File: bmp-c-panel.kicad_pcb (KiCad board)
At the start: 2 copper layers, 77 x 86 mm, 512 parts, among them J1 TYPE-C-31-M-12, J3 FTSH-107-01-F-DV-K, Q1 DMG1023UV, Q2 DMG1024UV, SW1 B3U-1000P, U1 USBLC6-2P6, U2 74LVC2T45GT, U3 74LVC2T45GT, U4 74LVC2T45GT, U5 74LVC2T45GT, U6 STM32F103CBU, U7 TLV70033DCK, Y1 CSTNE8M00G520000R0

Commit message: Fix up known issues.
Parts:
- removed the LOGO1 at (77.2, 28.2)
- removed the LOGO1 at (77.2, 46.8)
- removed the LOGO1 at (77.2, 65.2)
- removed the LOGO1 at (77.2, 83.8)
- removed the LOGO1 at (25.8, 83.8)
- removed the LOGO1 at (25.8, 65.2)
- removed the LOGO1 at (25.8, 46.8)
- removed the LOGO1 at (25.8, 28.2)
- removed the REF** at (83.0, 96.5)
- removed the REF** at (83.0, 15.5)
- removed the REF** at (20.0, 15.5)
- removed the REF** at (15.5, 96.5)
- removed the REF** at (87.5, 15.5)
- removed the REF** at (15.5, 15.5)
- added LOGO1: Logo_Open_Hardware_Small, Symbol:OSHW-Symbol_6.7x6mm_SilkScreen, B.Cu at (26.1, 28.2)
- added LOGO1: Logo_Open_Hardware_Small, Symbol:OSHW-Symbol_6.7x6mm_SilkScreen, B.Cu at (26.1, 46.8)
- added LOGO1: Logo_Open_Hardware_Small, Symbol:OSHW-Symbol_6.7x6mm_SilkScreen, B.Cu at (26.1, 65.2)
- added LOGO1: Logo_Open_Hardware_Small, Symbol:OSHW-Symbol_6.7x6mm_SilkScreen, B.Cu at (26.1, 83.8)
- added LOGO1: Logo_Open_Hardware_Small, Symbol:OSHW-Symbol_6.7x6mm_SilkScreen, B.Cu at (77.0, 28.2)
- added LOGO1: Logo_Open_Hardware_Small, Symbol:OSHW-Symbol_6.7x6mm_SilkScreen, B.Cu at (77.0, 46.8)
- added LOGO1: Logo_Open_Hardware_Small, Symbol:OSHW-Symbol_6.7x6mm_SilkScreen, B.Cu at (77.0, 65.2)
- added LOGO1: Logo_Open_Hardware_Small, Symbol:OSHW-Symbol_6.7x6mm_SilkScreen, B.Cu at (77.0, 83.8)
- added REF**: Fiducial_0.5mm_Mask1.5mm, Fiducial:Fiducial_0.5mm_Mask1.5mm, F.Cu at (82.0, 96.5)
- added REF**: Fiducial_0.5mm_Mask1.5mm, Fiducial:Fiducial_0.5mm_Mask1.5mm, F.Cu at (82.0, 15.5)
- added REF**: Fiducial_0.5mm_Mask1.5mm, Fiducial:Fiducial_0.5mm_Mask1.5mm, F.Cu at (21.0, 15.5)
- added REF**: MountingHole_3mm, MountingHole:MountingHole_3mm, F.Cu at (16.5, 96.0)
- added REF**: MountingHole_3mm, MountingHole:MountingHole_3mm, F.Cu at (86.5, 16.0)
- added REF**: MountingHole_3mm, MountingHole:MountingHole_3mm, F.Cu at (16.5, 16.0)
- D2 (x8): value LED GREEN -> LED BLUE
- D3 (x8): value LED ORANGE -> LED GREEN
- FB1 (x8): value Ferrite_Bead_Small -> 330R @ 100MHz
- moved REF** 1.12 mm to (86.5, 96.0)
- moved REF** 1.00 mm to (21.0, 96.5)
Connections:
- C1 pad 1: (no net) -> +3V3 (x7)
- C1 pad 2: (no net) -> GND (x7)
- C11 pad 1: (no net) -> /iTPWR (x7)
- C11 pad 2: (no net) -> GND (x7)
- C12 pad 1: (no net) -> Net-(C12-Pad1) (x7)
- C12 pad 2: (no net) -> GND (x7)
- C13 pad 1: (no net) -> GND (x7)
- C13 pad 2: (no net) -> /xTPWR (x7)
- C15 pad 1: (no net) -> +3V3 (x7)
- C15 pad 2: (no net) -> GND (x7)
- C16 pad 1: (no net) -> GND (x7)
- C16 pad 2: (no net) -> +3V3 (x7)
- C17 pad 1: (no net) -> GND (x7)
- C17 pad 2: (no net) -> +3V3 (x7)
- C18 pad 1: (no net) -> GND (x7)
- C18 pad 2: (no net) -> +3V3 (x7)
- C19 pad 1: (no net) -> GND (x7)
- C19 pad 2: (no net) -> /xTPWR (x7)
- C20 pad 1: (no net) -> GND (x7)
- C20 pad 2: (no net) -> +3V3 (x7)
- C21 pad 1: (no net) -> GND (x7)
- C21 pad 2: (no net) -> +3V3 (x7)
- C3 pad 1: (no net) -> +3V3 (x7)
- C3 pad 2: (no net) -> GND (x7)
- C4 pad 1: (no net) -> GND (x7)
- C4 pad 2: (no net) -> /xTPWR (x7)
- C5 pad 1: (no net) -> +5V (x7)
- C5 pad 2: (no net) -> GND (x7)
- C6 pad 1: (no net) -> +3V3 (x7)
- C6 pad 2: (no net) -> GND (x7)
- C7 pad 1: (no net) -> +5V (x7)
- C7 pad 2: (no net) -> GND (x7)
- C8 pad 1: (no net) -> GND (x7)
- C8 pad 2: (no net) -> /xTPWR (x7)
- C9 pad 1: (no net) -> +3V3 (x7)
- C9 pad 2: (no net) -> GND (x7)
- D1 pad 1: (no net) -> GND (x7)
- D1 pad 2: (no net) -> Net-(D1-Pad2) (x7)
- D2 pad 1: (no net) -> GND (x7)
- D2 pad 2: (no net) -> Net-(D2-Pad2) (x7)
- D3 pad 1: (no net) -> GND (x7)
- D3 pad 2: (no net) -> Net-(D3-Pad2) (x7)
- D4 pad 1: (no net) -> GND (x7)
- D4 pad 2: (no net) -> Net-(D4-Pad2) (x7)
- FB1 pad 1: (no net) -> +5V (x7)
- FB1 pad 2: (no net) -> Net-(FB1-Pad2) (x7)
- J1 pad A1: (no net) -> GND (x7)
- J1 pad A12: (no net) -> GND (x7)
- J1 pad A4: (no net) -> Net-(FB1-Pad2) (x7)
- J1 pad A5: (no net) -> Net-(J1-PadA5) (x7)
- J1 pad A6: (no net) -> /USBX_p (x7)
- J1 pad A7: (no net) -> /USBX_n (x7)
- J1 pad A8: (no net) -> Net-(J1-PadA8) (x7)
- J1 pad A9: (no net) -> Net-(FB1-Pad2) (x7)
- J1 pad B1: (no net) -> GND (x7)
- J1 pad B12: (no net) -> GND (x7)
- J1 pad B4: (no net) -> Net-(FB1-Pad2) (x7)
- J1 pad B5: (no net) -> Net-(J1-PadB5) (x7)
- J1 pad B6: (no net) -> /USBX_p (x7)
- J1 pad B7: (no net) -> /USBX_n (x7)
- J1 pad B8: (no net) -> Net-(J1-PadB8) (x7)
- J1 pad B9: (no net) -> Net-(FB1-Pad2) (x7)
- J1 pad S1: (no net) -> Net-(J1-PadS1) (x7)
- J3 pad 1: (no net) -> Net-(J3-Pad1) (x7)
- J3 pad 10: (no net) -> /TDI (x7)
- J3 pad 11: (no net) -> GND (x7)
- J3 pad 12: (no net) -> /RST (x7)
- J3 pad 13: (no net) -> /TXD (x7)
- J3 pad 14: (no net) -> /RXD (x7)
- J3 pad 2: (no net) -> Net-(J3-Pad2) (x7)
- J3 pad 3: (no net) -> /TPWR (x7)
- J3 pad 4: (no net) -> /TMS (x7)
- J3 pad 5: (no net) -> GND (x7)
- J3 pad 6: (no net) -> /TCK (x7)
- J3 pad 7: (no net) -> GND (x7)
- J3 pad 8: (no net) -> /TDO (x7)
- J3 pad 9: (no net) -> Net-(J3-Pad9) (x7)
- Q1 pad 1: (no net) -> Net-(Q1-Pad1) (x7)
- Q1 pad 2: (no net) -> /PWR_BR (x7)
- Q1 pad 3: (no net) -> /TPWR (x7)
- Q1 pad 4: (no net) -> Net-(Q1-Pad1) (x7)
- Q1 pad 5: (no net) -> /PWR_BR (x7)
- Q1 pad 6: (no net) -> +3V3 (x7)
- Q2 pad 1: (no net) -> GND (x7)
- Q2 pad 2: (no net) -> /iRST (x7)
- Q2 pad 3: (no net) -> /iRST_SENSE (x7)
- Q2 pad 4: (no net) -> GND (x7)
- Q2 pad 5: (no net) -> /xRST (x7)
- Q2 pad 6: (no net) -> /xRST (x7)
- R1 pad 1: (no net) -> GND (x7)
- R1 pad 2: (no net) -> Net-(J1-PadA5) (x7)
- R10 pad 1: (no net) -> /USBi_p (x7)
- R10 pad 2: (no net) -> Net-(R10-Pad2) (x7)
- R11 pad 1: (no net) -> /xRST (x7)
- R11 pad 2: (no net) -> /xTPWR (x7)
- R12 pad 1: (no net) -> /PWR_BR (x7)
- R12 pad 2: (no net) -> Net-(Q1-Pad1) (x7)
- R2 pad 1: (no net) -> GND (x7)
- R2 pad 2: (no net) -> Net-(J1-PadB5) (x7)
- R3 pad 1: (no net) -> /VBUS (x7)
- R3 pad 2: (no net) -> GND (x7)
- R4 pad 1: (no net) -> +5V (x7)
- R4 pad 2: (no net) -> /VBUS (x7)
- R5 pad 1: (no net) -> /USBi_n (x7)
- R5 pad 2: (no net) -> Net-(R5-Pad2) (x7)
- R6 pad 1: (no net) -> /USBi_p (x7)
- R6 pad 2: (no net) -> Net-(R6-Pad2) (x7)
- R7 pad 1: (no net) -> /iTPWR (x7)
- R7 pad 2: (no net) -> GND (x7)
- R8 pad 1: (no net) -> Net-(R8-Pad1) (x7)
- R8 pad 2: (no net) -> +3V3 (x7)
- R9 pad 1: (no net) -> /xTPWR (x7)
- R9 pad 2: (no net) -> /iTPWR (x7)
- RN1 pad 1: (no net) -> +3V3 (x7)
- RN1 pad 2: (no net) -> /LED2 (x7)
- RN1 pad 3: (no net) -> /LED1 (x7)
- RN1 pad 4: (no net) -> /LED0 (x7)
- RN1 pad 5: (no net) -> Net-(D4-Pad2) (x7)
- RN1 pad 6: (no net) -> Net-(D3-Pad2) (x7)
- RN1 pad 7: (no net) -> Net-(D1-Pad2) (x7)
- RN1 pad 8: (no net) -> Net-(D2-Pad2) (x7)
- RN2 pad 1: (no net) -> /RST (x7)
- RN2 pad 2: (no net) -> /RXD (x7)
- RN2 pad 3: (no net) -> /TMS (x7)
- RN2 pad 4: (no net) -> /TPWR (x7)
- RN2 pad 5: (no net) -> /xTPWR (x7)
- RN2 pad 6: (no net) -> /xTMS (x7)
- RN2 pad 7: (no net) -> /xRXD (x7)
- RN2 pad 8: (no net) -> /xRST (x7)
- RN3 pad 1: (no net) -> /TDO (x7)
- RN3 pad 2: (no net) -> /TDI (x7)
- RN3 pad 3: (no net) -> /TCK (x7)
- RN3 pad 4: (no net) -> /TXD (x7)
- RN3 pad 5: (no net) -> /xTXD (x7)
- RN3 pad 6: (no net) -> /xTCK (x7)
- RN3 pad 7: (no net) -> /xTDI (x7)
- RN3 pad 8: (no net) -> /xTDO (x7)
- SW1 pad 1: (no net) -> GND (x7)
- SW1 pad 2: (no net) -> Net-(R8-Pad1) (x7)
- TP1 pad 1: (no net) -> +3V3 (x7)
- TP2 pad 1: (no net) -> GND (x7)
- TP4 pad 1: (no net) -> Net-(C12-Pad1) (x7)
- TP5 pad 1: (no net) -> /SWDIO (x7)
- TP6 pad 1: (no net) -> /SWCLK (x7)
- U1 pad 1: (no net) -> /USBX_n (x7)
- U1 pad 2: (no net) -> GND (x7)
- U1 pad 3: (no net) -> /USBX_p (x7)
- U1 pad 4: (no net) -> Net-(R6-Pad2) (x7)
- U1 pad 5: (no net) -> +5V (x7)
- U1 pad 6: (no net) -> Net-(R5-Pad2) (x7)
- U2 pad 1: (no net) -> +3V3 (x7)
- U2 pad 2: (no net) -> GND (x7)
- U2 pad 3: (no net) -> /iTXD (x7)
- U2 pad 4: (no net) -> GND (x7)
- U2 pad 5: (no net) -> +3V3 (x7)
- U2 pad 6: (no net) -> /xTXD (x7)
- U2 pad 7: (no net) -> GND (x7)
- U2 pad 8: (no net) -> /xTPWR (x7)
- U3 pad 1: (no net) -> +3V3 (x7)
- U3 pad 2: (no net) -> /iTCK (x7)
- U3 pad 3: (no net) -> /iTDI (x7)
- U3 pad 4: (no net) -> GND (x7)
- U3 pad 5: (no net) -> +3V3 (x7)
- U3 pad 6: (no net) -> /xTDI (x7)
- U3 pad 7: (no net) -> /xTCK (x7)
- U3 pad 8: (no net) -> /xTPWR (x7)
- U4 pad 1: (no net) -> +3V3 (x7)
- U4 pad 2: (no net) -> /iTDO (x7)
- U4 pad 3: (no net) -> /iRXD (x7)
- U4 pad 4: (no net) -> GND (x7)
- U4 pad 5: (no net) -> GND (x7)
- U4 pad 6: (no net) -> /xRXD (x7)
- U4 pad 7: (no net) -> /xTDO (x7)
- U4 pad 8: (no net) -> /xTPWR (x7)
- U5 pad 1: (no net) -> +3V3 (x7)
- U5 pad 2: (no net) -> GND (x7)
- U5 pad 3: (no net) -> /iTMS (x7)
- U5 pad 4: (no net) -> GND (x7)
- U5 pad 5: (no net) -> /iTMS_DIR (x7)
- U5 pad 6: (no net) -> /xTMS (x7)
- U5 pad 7: (no net) -> GND (x7)
- U5 pad 8: (no net) -> /xTPWR (x7)
- U6 pad 1: (no net) -> +3V3 (x7)
- U6 pad 10: (no net) -> Net-(U6-Pad10) (x7)
- U6 pad 11: (no net) -> /iTMS_DIR (x7)
- U6 pad 12: (no net) -> /iRST (x7)
- U6 pad 13: (no net) -> /iTDI (x7)
- U6 pad 14: (no net) -> /iTMS (x7)
- U6 pad 15: (no net) -> /iTCK (x7)
- U6 pad 16: (no net) -> /iTDO (x7)
- U6 pad 17: (no net) -> /iRST_SENSE (x7)
- U6 pad 18: (no net) -> /iTPWR (x7)
- U6 pad 19: (no net) -> /PWR_BR (x7)
- U6 pad 2: (no net) -> Net-(U6-Pad2) (x7)
- U6 pad 20: (no net) -> /LED0 (x7)
- U6 pad 21: (no net) -> /LED1 (x7)
- U6 pad 22: (no net) -> /LED2 (x7)
- U6 pad 23: (no net) -> GND (x7)
- U6 pad 24: (no net) -> +3V3 (x7)
- U6 pad 25: (no net) -> Net-(R8-Pad1) (x7)
- U6 pad 26: (no net) -> /VBUS (x7)
- U6 pad 27: (no net) -> Net-(U6-Pad27) (x7)
- U6 pad 28: (no net) -> Net-(U6-Pad28) (x7)
- U6 pad 29: (no net) -> Net-(R10-Pad2) (x7)
- U6 pad 3: (no net) -> Net-(U6-Pad3) (x7)
- U6 pad 30: (no net) -> /iTXD (x7)
- U6 pad 31: (no net) -> /iRXD (x7)
- U6 pad 32: (no net) -> /USBi_n (x7)
- U6 pad 33: (no net) -> /USBi_p (x7)
- U6 pad 34: (no net) -> /SWDIO (x7)
- U6 pad 35: (no net) -> GND (x7)
- U6 pad 36: (no net) -> +3V3 (x7)
- U6 pad 37: (no net) -> /SWCLK (x7)
- U6 pad 38: (no net) -> Net-(U6-Pad38) (x7)
- U6 pad 39: (no net) -> Net-(U6-Pad39) (x7)
- U6 pad 4: (no net) -> Net-(U6-Pad4) (x7)
- U6 pad 40: (no net) -> +3V3 (x7)
- U6 pad 41: (no net) -> +3V3 (x7)
- U6 pad 42: (no net) -> +3V3 (x7)
- U6 pad 43: (no net) -> Net-(U6-Pad43) (x7)
- U6 pad 44: (no net) -> GND (x7)
- U6 pad 45: (no net) -> Net-(U6-Pad45) (x7)
- U6 pad 46: (no net) -> Net-(U6-Pad46) (x7)
- U6 pad 47: (no net) -> GND (x7)
- U6 pad 48: (no net) -> +3V3 (x7)
- U6 pad 49: (no net) -> GND (x7)
- U6 pad 5: (no net) -> Net-(U6-Pad5) (x7)
- U6 pad 6: (no net) -> Net-(U6-Pad6) (x7)
- U6 pad 7: (no net) -> Net-(C12-Pad1) (x7)
- U6 pad 8: (no net) -> GND (x7)
- U6 pad 9: (no net) -> +3V3 (x7)
- U7 pad 1: (no net) -> +5V (x7)
- U7 pad 2: (no net) -> GND (x7)
- U7 pad 3: (no net) -> +5V (x7)
- U7 pad 4: (no net) -> Net-(U7-Pad4) (x7)
- U7 pad 5: (no net) -> +3V3 (x7)
- Y1 pad 1: (no net) -> Net-(U6-Pad6) (x7)
- Y1 pad 2: (no net) -> GND (x7)
- Y1 pad 3: (no net) -> Net-(U6-Pad5) (x7)
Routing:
- net (no net): track 4864.6 -> 0.00 mm, vias 665 -> 0
- net +3V3: track 134.0 -> 1072.0 mm, vias 10 -> 80
- net GND: track 89.1 -> 712.5 mm, vias 42 -> 336
- net /iTXD: track 44.8 -> 358.7 mm, vias 4 -> 32
- net /xTPWR: track 34.9 -> 279.0 mm, vias 7 -> 56
- net Net-(R8-Pad1): track 28.6 -> 228.8 mm, vias 2 -> 16
- net Net-(C12-Pad1): track 27.6 -> 220.7 mm, vias 2 -> 16
- net /iRXD: track 26.4 -> 211.3 mm, vias 4 -> 32
- net /PWR_BR: track 25.9 -> 207.3 mm, vias 2 -> 16
- net +5V: track 16.4 -> 131.4 mm, vias 2 -> 16
- net /iRST_SENSE: track 16.3 -> 130.5 mm, vias 2 -> 16
- net /SWCLK: track 15.1 -> 120.5 mm, vias 1 -> 8
- net /RXD: track 13.6 -> 108.5 mm, vias 2 -> 16
- net /iRST: track 13.1 -> 105.0 mm, vias 2 -> 16
- net /RST: track 12.2 -> 97.2 mm, vias 2 -> 16
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- removed copper zone on B.Cu, net (none)

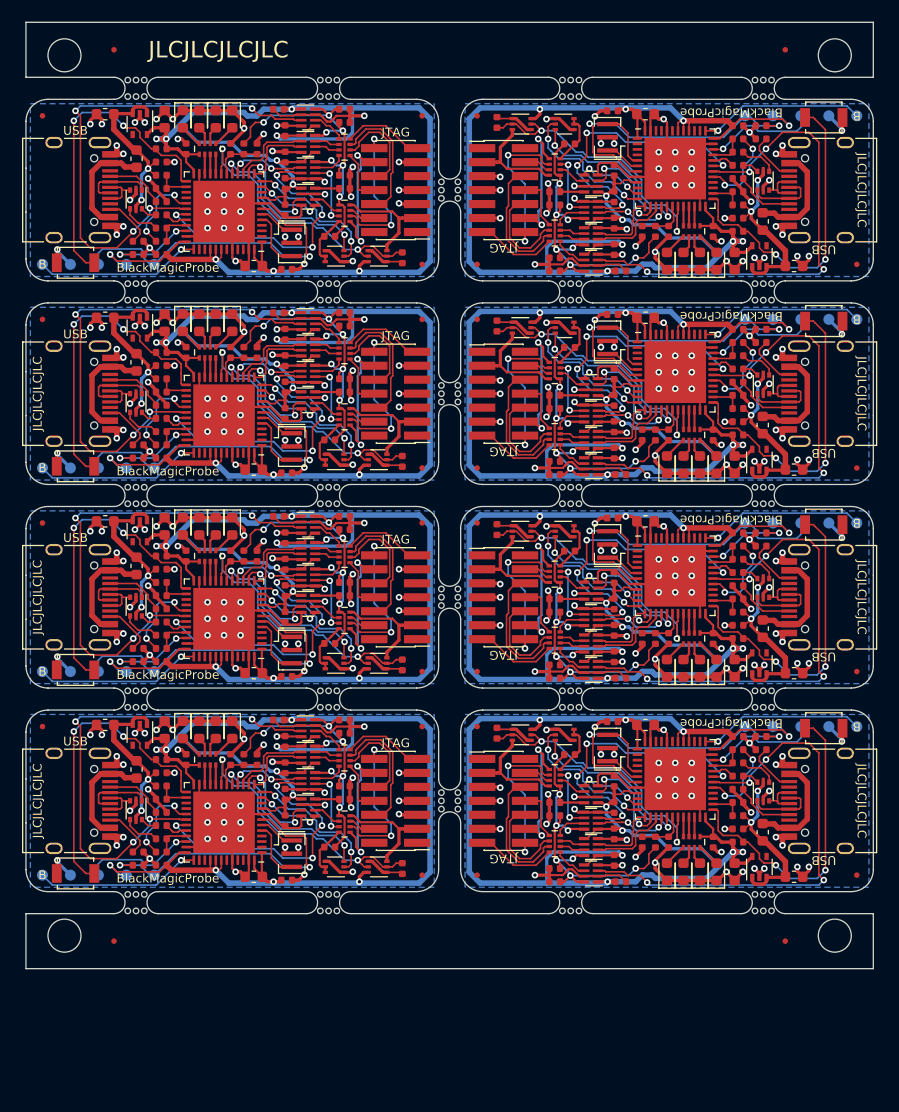
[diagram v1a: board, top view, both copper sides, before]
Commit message: Update alignment holes to be Stencil8 compatible.
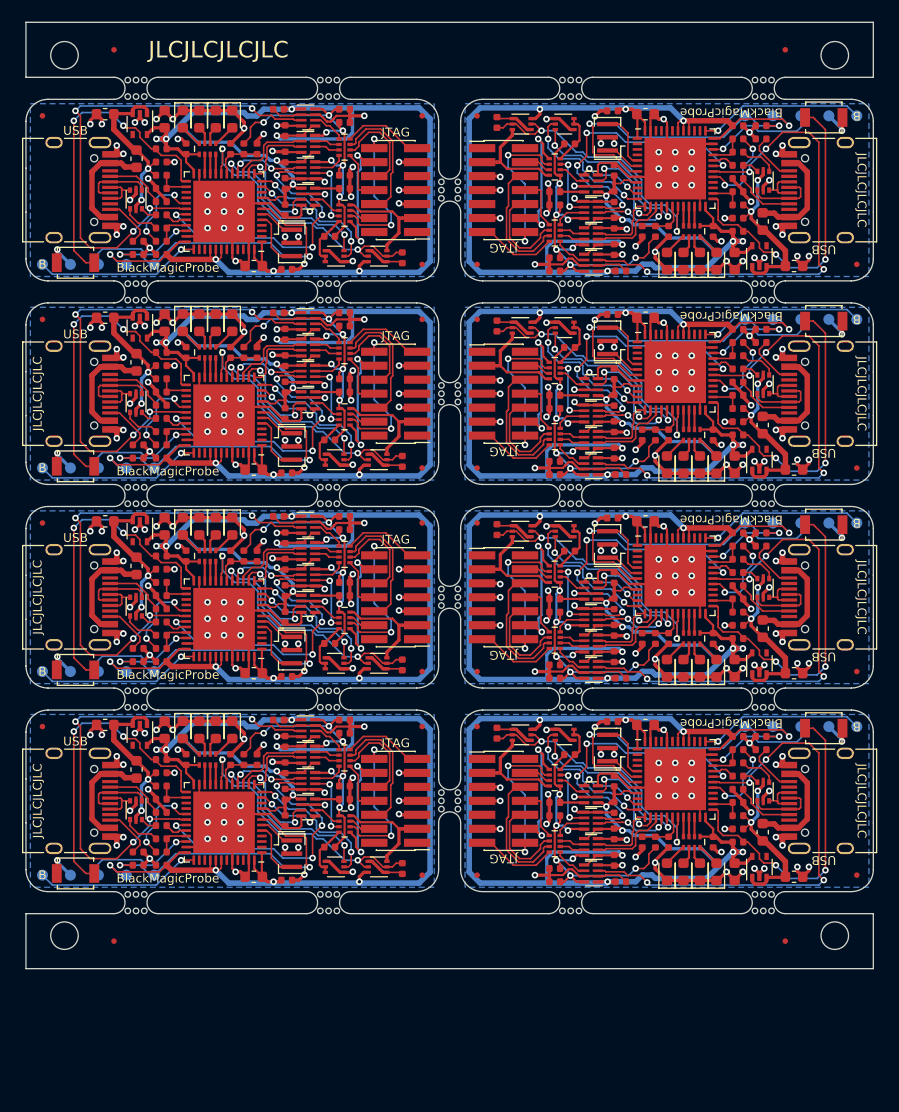
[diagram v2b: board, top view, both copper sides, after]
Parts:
- removed the REF** at (16.5, 96.0)
- removed the REF** at (86.5, 16.0)
- added REF**: MountingHole_2.5mm, MountingHole:MountingHole_2.5mm, F.Cu at (16.5, 96.0)
- added REF**: MountingHole_2.5mm, MountingHole:MountingHole_2.5mm, F.Cu at (86.5, 16.0)
- REF** (x2): value MountingHole_3mm -> MountingHole_2.5mm; footprint MountingHole:MountingHole_3mm -> MountingHole:MountingHole_2.5mm

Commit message: Moved panel alignment holes for easier assembly.
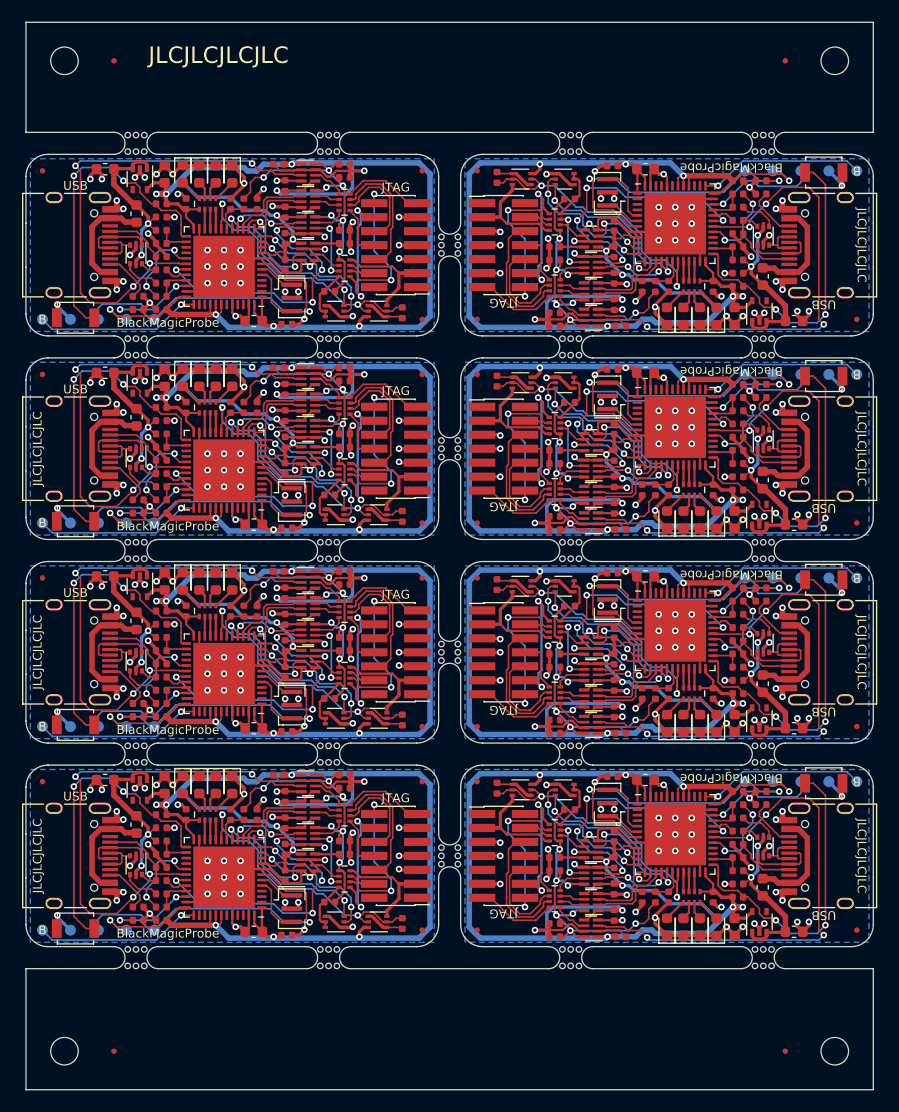
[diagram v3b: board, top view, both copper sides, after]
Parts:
- removed the C1 at (36.0, 39.4)
- removed the C1 at (36.0, 57.9)
- removed the C1 at (36.0, 76.4)
- removed the C1 at (67.0, 35.6)
- removed the C1 at (67.0, 54.1)
- removed the C1 at (67.0, 72.6)
- removed the C1 at (67.0, 91.1)
- removed the C11 at (31.6, 43.0)
- removed the C11 at (31.6, 61.5)
- removed the C11 at (31.6, 80.0)
- removed the C11 at (71.4, 32.0)
- removed the C11 at (71.4, 50.5)
- removed the C11 at (71.4, 69.0)
- removed the C11 at (71.4, 87.5)
- removed the C12 at (23.2, 52.6)
- removed the C12 at (23.2, 71.1)
- removed the C12 at (23.2, 89.6)
- removed the C12 at (79.8, 22.4)
- removed the C12 at (79.8, 40.9)
- removed the C12 at (79.8, 59.4)
- removed the C12 at (79.8, 77.9)
- removed the C13 at (42.0, 45.4)
- removed the C13 at (42.0, 63.9)
- removed the C13 at (42.0, 82.4)
- removed the C13 at (61.0, 29.6)
- removed the C13 at (61.0, 48.1)
- removed the C13 at (61.0, 66.6)
- removed the C13 at (61.0, 85.1)
- removed the C15 at (36.5, 46.1)
- removed the C15 at (36.5, 64.7)
- removed the C15 at (36.5, 83.2)
- removed the C15 at (66.5, 28.9)
- removed the C15 at (66.5, 47.4)
- removed the C15 at (66.5, 65.8)
- removed the C15 at (66.5, 84.3)
- removed the C16 at (25.3, 52.6)
- removed the C16 at (25.3, 71.1)
- removed the C16 at (25.3, 89.6)
- removed the C16 at (77.7, 22.4)
- removed the C16 at (77.7, 40.9)
- removed the C16 at (77.7, 59.4)
- removed the C16 at (77.7, 77.9)
- removed the C17 at (27.6, 43.0)
- removed the C17 at (27.6, 61.5)
- removed the C17 at (27.6, 80.0)
- removed the C17 at (75.5, 32.0)
- removed the C17 at (75.5, 50.5)
- removed the C17 at (75.5, 69.0)
- removed the C17 at (75.5, 87.5)
- removed the C18 at (36.5, 48.5)
- removed the C18 at (36.5, 67.0)
- removed the C18 at (36.5, 85.5)
- removed the C18 at (66.5, 26.4)
- removed the C18 at (66.5, 45.0)
- removed the C18 at (66.5, 63.5)
- removed the C18 at (66.5, 82.0)
- removed the C19 at (42.0, 46.6)
- removed the C19 at (42.0, 65.1)
- removed the C19 at (42.0, 83.6)
- removed the C19 at (61.0, 28.4)
- removed the C19 at (61.0, 46.9)
- removed the C19 at (61.0, 65.4)
- removed the C19 at (61.0, 83.9)
- removed the C20 at (36.7, 54.0)
- removed the C20 at (36.7, 72.5)
- removed the C20 at (36.7, 91.0)
- removed the C20 at (66.3, 21.1)
- removed the C20 at (66.3, 39.5)
- removed the C20 at (66.3, 58.0)
- removed the C20 at (66.3, 76.5)
- removed the C21 at (33.7, 53.6)
- removed the C21 at (33.7, 72.2)
- removed the C21 at (33.7, 90.7)
- removed the C21 at (69.3, 21.4)
- removed the C21 at (69.3, 39.9)
- removed the C21 at (69.3, 58.4)
- removed the C21 at (69.3, 76.8)
- removed the C3 at (25.6, 40.3)
- removed the C3 at (25.6, 58.8)
- removed the C3 at (25.6, 77.3)
- removed the C3 at (77.4, 34.7)
- removed the C3 at (77.4, 53.2)
- removed the C3 at (77.4, 71.7)
- removed the C3 at (77.4, 90.2)
- removed the C4 at (42.0, 39.4)
- removed the C4 at (42.0, 57.9)
- removed the C4 at (42.0, 76.4)
- removed the C4 at (61.0, 35.6)
- removed the C4 at (61.0, 54.1)
- removed the C4 at (61.0, 72.6)
- removed the C4 at (61.0, 91.1)
- removed the C5 at (25.3, 44.2)
- removed the C5 at (25.3, 62.7)
- removed the C5 at (25.3, 81.2)
- removed the C5 at (77.7, 30.8)
- removed the C5 at (77.7, 49.3)
- removed the C5 at (77.7, 67.8)
- removed the C5 at (77.7, 86.3)
- removed the C6 at (36.5, 41.4)
- removed the C6 at (36.5, 59.9)
- removed the C6 at (36.5, 78.3)
- removed the C6 at (66.5, 33.6)
- removed the C6 at (66.5, 52.1)
- removed the C6 at (66.5, 70.7)
- removed the C6 at (66.5, 89.2)
- removed the C7 at (20.2, 39.9)
- removed the C7 at (20.2, 58.4)
- removed the C7 at (20.2, 76.8)
- removed the C7 at (82.8, 35.1)
- removed the C7 at (82.8, 53.6)
- removed the C7 at (82.8, 72.2)
- removed the C7 at (82.8, 90.7)
- removed the C8 at (42.0, 40.6)
- removed the C8 at (42.0, 59.1)
- removed the C8 at (42.0, 77.6)
- removed the C8 at (61.0, 34.4)
- removed the C8 at (61.0, 52.9)
- removed the C8 at (61.0, 71.4)
- removed the C8 at (61.0, 89.9)
- removed the C9 at (36.5, 43.8)
- removed the C9 at (36.5, 62.2)
- removed the C9 at (36.5, 80.8)
- removed the C9 at (66.5, 31.2)
- removed the C9 at (66.5, 49.8)
- removed the C9 at (66.5, 68.2)
- removed the C9 at (66.5, 86.8)
- removed the D1 at (28.8, 40.3)
- removed the D1 at (28.8, 58.8)
- removed the D1 at (28.8, 77.3)
- removed the D1 at (74.2, 34.7)
- removed the D1 at (74.2, 53.2)
- removed the D1 at (74.2, 71.7)
- removed the D1 at (74.2, 90.2)
- removed the D2 at (27.2, 40.3)
- removed the D2 at (27.2, 58.8)
- removed the D2 at (27.2, 77.3)
- removed the D2 at (75.8, 34.7)
- removed the D2 at (75.8, 53.2)
- removed the D2 at (75.8, 71.7)
- removed the D2 at (75.8, 90.2)
- removed the D3 at (30.2, 40.3)
- removed the D3 at (30.2, 58.8)
- removed the D3 at (30.2, 77.3)
- removed the D3 at (72.8, 34.7)
- removed the D3 at (72.8, 53.2)
- removed the D3 at (72.8, 71.7)
- removed the D3 at (72.8, 90.2)
- removed the D4 at (31.8, 40.3)
- removed the D4 at (31.8, 58.8)
- removed the D4 at (31.8, 77.3)
- removed the D4 at (71.2, 34.7)
- removed the D4 at (71.2, 53.2)
- removed the D4 at (71.2, 71.7)
- removed the D4 at (71.2, 90.2)
- removed the FB1 at (23.1, 43.9)
- removed the FB1 at (23.1, 62.4)
- removed the FB1 at (23.1, 80.9)
- removed the FB1 at (80.0, 31.1)
- removed the FB1 at (80.0, 49.6)
- removed the FB1 at (80.0, 68.1)
- removed the FB1 at (80.0, 86.6)
- removed the FID1 at (14.5, 40.0)
- removed the FID1 at (14.5, 58.5)
- removed the FID1 at (14.5, 77.0)
- removed the FID1 at (88.5, 35.0)
- removed the FID1 at (88.5, 53.5)
- removed the FID1 at (88.5, 72.0)
- removed the FID1 at (88.5, 90.5)
- removed the FID2 at (49.0, 40.0)
- removed the FID2 at (49.0, 58.5)
- removed the FID2 at (49.0, 77.0)
- removed the FID2 at (54.0, 35.0)
- removed the FID2 at (54.0, 53.5)
- removed the FID2 at (54.0, 72.0)
- removed the FID2 at (54.0, 90.5)
- removed the FID3 at (49.0, 53.5)
- removed the FID3 at (49.0, 72.0)
- removed the FID3 at (49.0, 90.5)
- removed the FID3 at (54.0, 21.5)
- removed the FID3 at (54.0, 40.0)
- removed the FID3 at (54.0, 58.5)
- removed the FID3 at (54.0, 77.0)
- removed the J1 at (16.6, 46.8)
- removed the J1 at (16.6, 65.2)
- removed the J1 at (16.6, 83.8)
- removed the J1 at (86.4, 28.2)
- removed the J1 at (86.4, 46.8)
- removed the J1 at (86.4, 65.2)
- removed the J1 at (86.4, 83.8)
- removed the J3 at (46.6, 46.8)
- removed the J3 at (46.6, 65.2)
- removed the J3 at (46.6, 83.8)
- removed the J3 at (56.4, 28.2)
- removed the J3 at (56.4, 46.8)
- removed the J3 at (56.4, 65.2)
- removed the J3 at (56.4, 83.8)
- removed the LOGO1 at (26.1, 46.8)
- removed the LOGO1 at (26.1, 65.2)
- removed the LOGO1 at (26.1, 83.8)
- removed the LOGO1 at (77.0, 28.2)
- removed the LOGO1 at (77.0, 46.8)
- removed the LOGO1 at (77.0, 65.2)
- removed the LOGO1 at (77.0, 83.8)
- removed the Q1 at (45.0, 52.8)
- removed the Q1 at (45.0, 71.2)
- removed the Q1 at (45.0, 89.8)
- removed the Q1 at (58.0, 22.2)
- removed the Q1 at (58.0, 40.8)
- removed the Q1 at (58.0, 59.2)
- removed the Q1 at (58.0, 77.8)
- removed the Q2 at (41.0, 52.8)
- removed the Q2 at (41.0, 71.2)
- removed the Q2 at (41.0, 89.8)
- removed the Q2 at (62.0, 22.2)
- removed the Q2 at (62.0, 40.8)
- removed the Q2 at (62.0, 59.2)
- removed the Q2 at (62.0, 77.8)
- removed the R1 at (25.3, 47.8)
- removed the R1 at (25.3, 66.3)
- removed the R1 at (25.3, 84.8)
- removed the R1 at (77.7, 27.2)
- removed the R1 at (77.7, 45.7)
- removed the R1 at (77.7, 64.2)
- removed the R1 at (77.7, 82.7)
- removed the R10 at (25.3, 51.4)
- removed the R10 at (25.3, 69.9)
- removed the R10 at (25.3, 88.4)
- removed the R10 at (77.7, 23.6)
- removed the R10 at (77.7, 42.1)
- removed the R10 at (77.7, 60.6)
- removed the R10 at (77.7, 79.1)
- removed the R11 at (40.6, 51.0)
- removed the R11 at (40.6, 69.5)
- removed the R11 at (40.6, 88.0)
- removed the R11 at (62.4, 24.1)
- removed the R11 at (62.4, 42.5)
- removed the R11 at (62.4, 61.0)
- removed the R11 at (62.4, 79.5)
- removed the R12 at (47.2, 52.9)
- removed the R12 at (47.2, 71.4)
- removed the R12 at (47.2, 89.9)
- removed the R12 at (55.8, 22.1)
- removed the R12 at (55.8, 40.6)
- removed the R12 at (55.8, 59.1)
- removed the R12 at (55.8, 77.6)
- removed the R2 at (23.2, 51.4)
- removed the R2 at (23.2, 69.9)
- removed the R2 at (23.2, 88.4)
- removed the R2 at (79.8, 23.6)
- removed the R2 at (79.8, 42.1)
- removed the R2 at (79.8, 60.6)
- removed the R2 at (79.8, 79.1)
- removed the R3 at (25.3, 46.6)
- removed the R3 at (25.3, 65.1)
- removed the R3 at (25.3, 83.6)
- removed the R3 at (77.7, 28.4)
- removed the R3 at (77.7, 46.9)
- removed the R3 at (77.7, 65.4)
- removed the R3 at (77.7, 83.9)
- removed the R4 at (25.3, 45.4)
- removed the R4 at (25.3, 63.9)
- removed the R4 at (25.3, 82.4)
- removed the R4 at (77.7, 29.6)
- removed the R4 at (77.7, 48.1)
- removed the R4 at (77.7, 66.6)
- removed the R4 at (77.7, 85.1)
- removed the R5 at (25.3, 49.0)
- removed the R5 at (25.3, 67.5)
- removed the R5 at (25.3, 86.0)
- removed the R5 at (77.7, 26.0)
- removed the R5 at (77.7, 44.5)
- removed the R5 at (77.7, 63.0)
- removed the R5 at (77.7, 81.5)
- removed the R6 at (25.3, 50.2)
- removed the R6 at (25.3, 68.7)
- removed the R6 at (25.3, 87.2)
- removed the R6 at (77.7, 24.8)
- removed the R6 at (77.7, 43.3)
- removed the R6 at (77.7, 61.8)
- removed the R6 at (77.7, 80.3)
- removed the R7 at (34.0, 43.0)
- removed the R7 at (34.0, 61.5)
- removed the R7 at (34.0, 80.0)
- removed the R7 at (69.0, 32.0)
- removed the R7 at (69.0, 50.5)
- removed the R7 at (69.0, 69.0)
- removed the R7 at (69.0, 87.5)
- removed the R8 at (25.3, 43.0)
- removed the R8 at (25.3, 61.5)
- removed the R8 at (25.3, 80.0)
- removed the R8 at (77.7, 32.0)
- removed the R8 at (77.7, 50.5)
- removed the R8 at (77.7, 69.0)
- removed the R8 at (77.7, 87.5)
- removed the R9 at (32.8, 43.0)
- removed the R9 at (32.8, 61.5)
- removed the R9 at (32.8, 80.0)
- removed the R9 at (70.2, 32.0)
- removed the R9 at (70.2, 50.5)
- removed the R9 at (70.2, 69.0)
- removed the R9 at (70.2, 87.5)
- removed the REF** at (16.5, 96.0)
- removed the REF** at (86.5, 16.0)
- removed the REF** at (82.0, 96.5)
- removed the REF** at (82.0, 15.5)
- removed the REF** at (21.0, 15.5)
- removed the RN1 at (29.5, 43.0)
- removed the RN1 at (29.5, 61.5)
- removed the RN1 at (29.5, 80.0)
- removed the RN1 at (73.5, 32.0)
- removed the RN1 at (73.5, 50.5)
- removed the RN1 at (73.5, 69.0)
- removed the RN1 at (73.5, 87.5)
- removed the RN2 at (42.0, 48.9)
- removed the RN2 at (42.0, 67.3)
- removed the RN2 at (42.0, 85.8)
- removed the RN2 at (61.0, 26.1)
- removed the RN2 at (61.0, 44.6)
- removed the RN2 at (61.0, 63.1)
- removed the RN2 at (61.0, 81.7)
- removed the RN3 at (42.0, 42.9)
- removed the RN3 at (42.0, 61.4)
- removed the RN3 at (42.0, 79.8)
- removed the RN3 at (61.0, 32.1)
- removed the RN3 at (61.0, 50.6)
- removed the RN3 at (61.0, 69.2)
- removed the RN3 at (61.0, 87.7)
- removed the SW1 at (17.5, 53.4)
- removed the SW1 at (17.5, 71.8)
- removed the SW1 at (17.5, 90.3)
- removed the SW1 at (85.5, 21.6)
- removed the SW1 at (85.5, 40.1)
- removed the SW1 at (85.5, 58.6)
- removed the SW1 at (85.5, 77.2)
- removed the TP1 at (22.1, 53.5)
- removed the TP1 at (22.1, 72.0)
- removed the TP1 at (22.1, 90.5)
- removed the TP1 at (80.9, 21.5)
- removed the TP1 at (80.9, 40.0)
- removed the TP1 at (80.9, 58.5)
- removed the TP1 at (80.9, 77.0)
- removed the TP2 at (17.0, 53.5)
- removed the TP2 at (17.0, 72.0)
- removed the TP2 at (17.0, 90.5)
- removed the TP2 at (86.0, 21.5)
- removed the TP2 at (86.0, 40.0)
- removed the TP2 at (86.0, 58.5)
- removed the TP2 at (86.0, 77.0)
- removed the TP4 at (24.7, 53.5)
- removed the TP4 at (24.7, 72.0)
- removed the TP4 at (24.7, 90.5)
- removed the TP4 at (78.3, 21.5)
- removed the TP4 at (78.3, 40.0)
- removed the TP4 at (78.3, 58.5)
- removed the TP4 at (78.3, 77.0)
- removed the TP5 at (19.6, 53.5)
- removed the TP5 at (19.6, 72.0)
- removed the TP5 at (19.6, 90.5)
- removed the TP5 at (83.4, 21.5)
- removed the TP5 at (83.4, 40.0)
- removed the TP5 at (83.4, 58.5)
- removed the TP5 at (83.4, 77.0)
- removed the TP6 at (14.5, 53.5)
- removed the TP6 at (14.5, 72.0)
- removed the TP6 at (14.5, 90.5)
- removed the TP6 at (88.5, 21.5)
- removed the TP6 at (88.5, 40.0)
- removed the TP6 at (88.5, 58.5)
- removed the TP6 at (88.5, 77.0)
- removed the U1 at (23.0, 47.6)
- removed the U1 at (23.0, 66.1)
- removed the U1 at (23.0, 84.6)
- removed the U1 at (80.0, 27.4)
- removed the U1 at (80.0, 45.9)
- removed the U1 at (80.0, 64.4)
- removed the U1 at (80.0, 82.9)
- removed the U2 at (38.6, 40.1)
- removed the U2 at (38.6, 58.6)
- removed the U2 at (38.6, 77.2)
- removed the U2 at (64.3, 34.9)
- removed the U2 at (64.3, 53.4)
- removed the U2 at (64.3, 71.8)
- removed the U2 at (64.3, 90.3)
- removed the U3 at (38.6, 42.5)
- removed the U3 at (38.6, 61.0)
- removed the U3 at (38.6, 79.5)
- removed the U3 at (64.3, 32.5)
- removed the U3 at (64.3, 51.0)
- removed the U3 at (64.3, 69.5)
- removed the U3 at (64.3, 88.0)
- removed the U4 at (38.6, 45.0)
- removed the U4 at (38.6, 63.5)
- removed the U4 at (38.6, 82.0)
- removed the U4 at (64.3, 30.1)
- removed the U4 at (64.3, 48.5)
- removed the U4 at (64.3, 67.0)
- removed the U4 at (64.3, 85.5)
- removed the U5 at (38.6, 47.4)
- removed the U5 at (38.6, 65.8)
- removed the U5 at (38.6, 84.3)
- removed the U5 at (64.3, 27.6)
- removed the U5 at (64.3, 46.1)
- removed the U5 at (64.3, 64.7)
- removed the U5 at (64.3, 83.2)
- removed the U6 at (31.0, 48.7)
- removed the U6 at (31.0, 67.2)
- removed the U6 at (31.0, 85.7)
- removed the U6 at (72.0, 26.3)
- removed the U6 at (72.0, 44.8)
- removed the U6 at (72.0, 63.3)
- removed the U6 at (72.0, 81.8)
- removed the U7 at (23.4, 40.8)
- removed the U7 at (23.4, 59.2)
- removed the U7 at (23.4, 77.8)
- removed the U7 at (79.7, 34.2)
- removed the U7 at (79.7, 52.8)
- removed the U7 at (79.7, 71.2)
- removed the U7 at (79.7, 89.8)
- removed the Y1 at (37.1, 51.5)
- removed the Y1 at (37.1, 70.0)
- removed the Y1 at (37.1, 88.5)
- removed the Y1 at (65.8, 23.4)
- removed the Y1 at (65.8, 42.0)
- removed the Y1 at (65.8, 60.5)
- removed the Y1 at (65.8, 79.0)
- removed the mouse-bite-2mm-slot at (40.5, 74.5)
- removed the mouse-bite-2mm-slot at (23.0, 56.0)
- removed the mouse-bite-2mm-slot at (40.5, 56.0)
- removed the mouse-bite-2mm-slot at (51.5, 46.8)
- removed the mouse-bite-2mm-slot at (23.0, 37.5)
- removed the mouse-bite-2mm-slot at (40.5, 37.5)
- removed the mouse-bite-2mm-slot at (23.0, 93.0)
- removed the mouse-bite-2mm-slot at (62.5, 19.0)
- removed the mouse-bite-2mm-slot at (80.0, 19.0)
- removed the mouse-bite-2mm-slot at (40.5, 93.0)
- removed the mouse-bite-2mm-slot at (51.5, 83.8)
- removed the mouse-bite-2mm-slot at (23.0, 74.5)
- added C1: 100n, Capacitor_SMD:C_0402_1005Metric, F.Cu at (36.0, 44.4)
- added C1: 100n, Capacitor_SMD:C_0402_1005Metric, F.Cu at (36.0, 62.9)
- added C1: 100n, Capacitor_SMD:C_0402_1005Metric, F.Cu at (36.0, 81.4)
- added C1: 100n, Capacitor_SMD:C_0402_1005Metric, F.Cu at (67.0, 40.6)
- added C1: 100n, Capacitor_SMD:C_0402_1005Metric, F.Cu at (67.0, 59.1)
- added C1: 100n, Capacitor_SMD:C_0402_1005Metric, F.Cu at (67.0, 77.6)
- added C1: 100n, Capacitor_SMD:C_0402_1005Metric, F.Cu at (67.0, 96.1)
- added C11: 100n, Capacitor_SMD:C_0402_1005Metric, F.Cu at (31.6, 48.0)
- added C11: 100n, Capacitor_SMD:C_0402_1005Metric, F.Cu at (31.6, 66.5)
- added C11: 100n, Capacitor_SMD:C_0402_1005Metric, F.Cu at (31.6, 85.0)
- added C11: 100n, Capacitor_SMD:C_0402_1005Metric, F.Cu at (71.4, 37.0)
- added C11: 100n, Capacitor_SMD:C_0402_1005Metric, F.Cu at (71.4, 55.5)
- added C11: 100n, Capacitor_SMD:C_0402_1005Metric, F.Cu at (71.4, 74.0)
- added C11: 100n, Capacitor_SMD:C_0402_1005Metric, F.Cu at (71.4, 92.5)
- added C12: 100n, Capacitor_SMD:C_0402_1005Metric, F.Cu at (23.2, 57.6)
- added C12: 100n, Capacitor_SMD:C_0402_1005Metric, F.Cu at (23.2, 76.1)
- added C12: 100n, Capacitor_SMD:C_0402_1005Metric, F.Cu at (23.2, 94.6)
- added C12: 100n, Capacitor_SMD:C_0402_1005Metric, F.Cu at (79.8, 27.4)
- added C12: 100n, Capacitor_SMD:C_0402_1005Metric, F.Cu at (79.8, 45.9)
- added C12: 100n, Capacitor_SMD:C_0402_1005Metric, F.Cu at (79.8, 64.4)
- added C12: 100n, Capacitor_SMD:C_0402_1005Metric, F.Cu at (79.8, 82.9)
- added C13: 100n, Capacitor_SMD:C_0402_1005Metric, F.Cu at (42.0, 50.4)
- added C13: 100n, Capacitor_SMD:C_0402_1005Metric, F.Cu at (42.0, 68.9)
- added C13: 100n, Capacitor_SMD:C_0402_1005Metric, F.Cu at (42.0, 87.4)
- added C13: 100n, Capacitor_SMD:C_0402_1005Metric, F.Cu at (61.0, 34.6)
- added C13: 100n, Capacitor_SMD:C_0402_1005Metric, F.Cu at (61.0, 53.1)
- added C13: 100n, Capacitor_SMD:C_0402_1005Metric, F.Cu at (61.0, 71.6)
- added C13: 100n, Capacitor_SMD:C_0402_1005Metric, F.Cu at (61.0, 90.1)
- added C15: 100n, Capacitor_SMD:C_0402_1005Metric, F.Cu at (36.5, 51.1)
- added C15: 100n, Capacitor_SMD:C_0402_1005Metric, F.Cu at (36.5, 69.7)
- added C15: 100n, Capacitor_SMD:C_0402_1005Metric, F.Cu at (36.5, 88.2)
- added C15: 100n, Capacitor_SMD:C_0402_1005Metric, F.Cu at (66.5, 33.9)
- added C15: 100n, Capacitor_SMD:C_0402_1005Metric, F.Cu at (66.5, 52.4)
- added C15: 100n, Capacitor_SMD:C_0402_1005Metric, F.Cu at (66.5, 70.8)
- added C15: 100n, Capacitor_SMD:C_0402_1005Metric, F.Cu at (66.5, 89.3)
- added C16: 100n, Capacitor_SMD:C_0402_1005Metric, F.Cu at (25.3, 57.6)
- added C16: 100n, Capacitor_SMD:C_0402_1005Metric, F.Cu at (25.3, 76.1)
- added C16: 100n, Capacitor_SMD:C_0402_1005Metric, F.Cu at (25.3, 94.6)
- added C16: 100n, Capacitor_SMD:C_0402_1005Metric, F.Cu at (77.7, 27.4)
- added C16: 100n, Capacitor_SMD:C_0402_1005Metric, F.Cu at (77.7, 45.9)
- added C16: 100n, Capacitor_SMD:C_0402_1005Metric, F.Cu at (77.7, 64.4)
- added C16: 100n, Capacitor_SMD:C_0402_1005Metric, F.Cu at (77.7, 82.9)
- added C17: 100n, Capacitor_SMD:C_0402_1005Metric, F.Cu at (27.6, 48.0)
- added C17: 100n, Capacitor_SMD:C_0402_1005Metric, F.Cu at (27.6, 66.5)
- added C17: 100n, Capacitor_SMD:C_0402_1005Metric, F.Cu at (27.6, 85.0)
- added C17: 100n, Capacitor_SMD:C_0402_1005Metric, F.Cu at (75.5, 37.0)
- added C17: 100n, Capacitor_SMD:C_0402_1005Metric, F.Cu at (75.5, 55.5)
- added C17: 100n, Capacitor_SMD:C_0402_1005Metric, F.Cu at (75.5, 74.0)
- added C17: 100n, Capacitor_SMD:C_0402_1005Metric, F.Cu at (75.5, 92.5)
- added C18: 100n, Capacitor_SMD:C_0402_1005Metric, F.Cu at (36.5, 53.5)
- added C18: 100n, Capacitor_SMD:C_0402_1005Metric, F.Cu at (36.5, 72.0)
- added C18: 100n, Capacitor_SMD:C_0402_1005Metric, F.Cu at (36.5, 90.5)
- added C18: 100n, Capacitor_SMD:C_0402_1005Metric, F.Cu at (66.5, 31.4)
- added C18: 100n, Capacitor_SMD:C_0402_1005Metric, F.Cu at (66.5, 50.0)
- added C18: 100n, Capacitor_SMD:C_0402_1005Metric, F.Cu at (66.5, 68.5)
- added C18: 100n, Capacitor_SMD:C_0402_1005Metric, F.Cu at (66.5, 87.0)
- added C19: 100n, Capacitor_SMD:C_0402_1005Metric, F.Cu at (42.0, 51.6)
- added C19: 100n, Capacitor_SMD:C_0402_1005Metric, F.Cu at (42.0, 70.1)
- added C19: 100n, Capacitor_SMD:C_0402_1005Metric, F.Cu at (42.0, 88.6)
- added C19: 100n, Capacitor_SMD:C_0402_1005Metric, F.Cu at (61.0, 33.4)
- added C19: 100n, Capacitor_SMD:C_0402_1005Metric, F.Cu at (61.0, 51.9)
- added C19: 100n, Capacitor_SMD:C_0402_1005Metric, F.Cu at (61.0, 70.4)
- added C19: 100n, Capacitor_SMD:C_0402_1005Metric, F.Cu at (61.0, 88.9)
- added C20: 100n, Capacitor_SMD:C_0402_1005Metric, F.Cu at (36.7, 59.0)
- added C20: 100n, Capacitor_SMD:C_0402_1005Metric, F.Cu at (36.7, 77.5)
- added C20: 100n, Capacitor_SMD:C_0402_1005Metric, F.Cu at (36.7, 96.0)
- added C20: 100n, Capacitor_SMD:C_0402_1005Metric, F.Cu at (66.3, 26.1)
- added C20: 100n, Capacitor_SMD:C_0402_1005Metric, F.Cu at (66.3, 44.5)
- added C20: 100n, Capacitor_SMD:C_0402_1005Metric, F.Cu at (66.3, 63.0)
- added C20: 100n, Capacitor_SMD:C_0402_1005Metric, F.Cu at (66.3, 81.5)
- added C21: 4u7, Capacitor_SMD:C_0603_1608Metric, F.Cu at (33.7, 58.6)
- added C21: 4u7, Capacitor_SMD:C_0603_1608Metric, F.Cu at (33.7, 77.2)
- added C21: 4u7, Capacitor_SMD:C_0603_1608Metric, F.Cu at (33.7, 95.7)
- added C21: 4u7, Capacitor_SMD:C_0603_1608Metric, F.Cu at (69.3, 26.4)
- added C21: 4u7, Capacitor_SMD:C_0603_1608Metric, F.Cu at (69.3, 44.9)
- added C21: 4u7, Capacitor_SMD:C_0603_1608Metric, F.Cu at (69.3, 63.4)
- added C21: 4u7, Capacitor_SMD:C_0603_1608Metric, F.Cu at (69.3, 81.8)
- added C3: 4u7, Capacitor_SMD:C_0603_1608Metric, F.Cu at (25.6, 45.3)
- added C3: 4u7, Capacitor_SMD:C_0603_1608Metric, F.Cu at (25.6, 63.8)
- added C3: 4u7, Capacitor_SMD:C_0603_1608Metric, F.Cu at (25.6, 82.3)
- added C3: 4u7, Capacitor_SMD:C_0603_1608Metric, F.Cu at (77.4, 39.7)
- added C3: 4u7, Capacitor_SMD:C_0603_1608Metric, F.Cu at (77.4, 58.2)
- added C3: 4u7, Capacitor_SMD:C_0603_1608Metric, F.Cu at (77.4, 76.7)
- added C3: 4u7, Capacitor_SMD:C_0603_1608Metric, F.Cu at (77.4, 95.2)
- added C4: 100n, Capacitor_SMD:C_0402_1005Metric, F.Cu at (42.0, 44.4)
- added C4: 100n, Capacitor_SMD:C_0402_1005Metric, F.Cu at (42.0, 62.9)
- added C4: 100n, Capacitor_SMD:C_0402_1005Metric, F.Cu at (42.0, 81.4)
- added C4: 100n, Capacitor_SMD:C_0402_1005Metric, F.Cu at (61.0, 40.6)
- added C4: 100n, Capacitor_SMD:C_0402_1005Metric, F.Cu at (61.0, 59.1)
- added C4: 100n, Capacitor_SMD:C_0402_1005Metric, F.Cu at (61.0, 77.6)
- added C4: 100n, Capacitor_SMD:C_0402_1005Metric, F.Cu at (61.0, 96.1)
- added C5: 100n, Capacitor_SMD:C_0402_1005Metric, F.Cu at (25.3, 49.2)
- added C5: 100n, Capacitor_SMD:C_0402_1005Metric, F.Cu at (25.3, 67.7)
- added C5: 100n, Capacitor_SMD:C_0402_1005Metric, F.Cu at (25.3, 86.2)
- added C5: 100n, Capacitor_SMD:C_0402_1005Metric, F.Cu at (77.7, 35.8)
- added C5: 100n, Capacitor_SMD:C_0402_1005Metric, F.Cu at (77.7, 54.3)
- added C5: 100n, Capacitor_SMD:C_0402_1005Metric, F.Cu at (77.7, 72.8)
- added C5: 100n, Capacitor_SMD:C_0402_1005Metric, F.Cu at (77.7, 91.3)
- added C6: 100n, Capacitor_SMD:C_0402_1005Metric, F.Cu at (36.5, 46.4)
- added C6: 100n, Capacitor_SMD:C_0402_1005Metric, F.Cu at (36.5, 64.8)
- added C6: 100n, Capacitor_SMD:C_0402_1005Metric, F.Cu at (36.5, 83.3)
- added C6: 100n, Capacitor_SMD:C_0402_1005Metric, F.Cu at (66.5, 38.6)
- added C6: 100n, Capacitor_SMD:C_0402_1005Metric, F.Cu at (66.5, 57.1)
- added C6: 100n, Capacitor_SMD:C_0402_1005Metric, F.Cu at (66.5, 75.7)
- added C6: 100n, Capacitor_SMD:C_0402_1005Metric, F.Cu at (66.5, 94.2)
- added C7: 4u7, Capacitor_SMD:C_0603_1608Metric, F.Cu at (20.2, 44.9)
- added C7: 4u7, Capacitor_SMD:C_0603_1608Metric, F.Cu at (20.2, 63.4)
- added C7: 4u7, Capacitor_SMD:C_0603_1608Metric, F.Cu at (20.2, 81.8)
- added C7: 4u7, Capacitor_SMD:C_0603_1608Metric, F.Cu at (82.8, 40.1)
- added C7: 4u7, Capacitor_SMD:C_0603_1608Metric, F.Cu at (82.8, 58.6)
- added C7: 4u7, Capacitor_SMD:C_0603_1608Metric, F.Cu at (82.8, 77.2)
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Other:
- board size 77 x 86 mm -> 77 x 97 mm
